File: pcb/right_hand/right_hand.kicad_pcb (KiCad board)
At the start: 2 copper layers, 160 x 110 mm, 113 parts, among them J0 UJ20-C-H-G-SMT-P16-TR, U0 SW_Push

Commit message: Fix Bluetooh Enable positioning
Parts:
- moved BLUETOOTH 0.30 mm to (190.0, 144.6)
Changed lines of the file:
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@@
 		(at 219.2375 144.6)
 		(property "Reference" "PROTOCOL"
-			(at -0.0375 -3.27 0)
+			(at -0.0375 -3.4 0)
 			(layer "F.SilkS")
 			(effects
@@
 	(footprint "snap_magic_footprints:SW_SLW-864587-2A-RA-N-D"
 		(layer "F.Cu")
-		(at 190.0375 144.3)
+		(at 190.0375 144.6)
 		(property "Reference" "BLUETOOTH"
 			(at 0.0725 -3.44 0)
@@
 	)
 	(segment
+		(start 188.0375 144.6)
+		(end 188.0375 134.6375)
+		(width 0.2)
+		(layer "F.Cu")
+		(net 80)
+	)
+	(segment
 		(start 214.4 131.2)
 		(end 217.2375 134.0375)
@@
 	)
 	(segment
-		(start 188.0375 134.6375)
-		(end 188.0375 144.3)
-		(width 0.2)
-		(layer "F.Cu")
-		(net 80)
-	)
-	(segment
 		(start 217.2375 134.0375)
 		(end 217.2375 144.6)
@@
 	)
 	(segment
-		(start 182.8 136.4)
+		(start 190.0375 144.6)
 		(end 190.0375 143.6375)
 		(width 0.2)
@@
 	)
 	(segment
-		(start 190.0375 143.6375)
-		(end 190.0375 144.3)
+		(start 182.8 136.4)
+		(end 190.0375 143.6375)
 		(width 0.2)
 		(layer "B.Cu")
@@
 			)
 		)
+	)
+	(zone
+		(net 0)
+		(net_name "")
+		(layers "F.Cu" "B.Cu")
+		(hatch edge 0.5)
+		(connect_pads
+			(clearance 0)
+		)
+		(min_thickness 0.25)
+		(filled_areas_thickness no)
+		(keepout
+			(tracks allowed)
+			(vias allowed)
+			(pads allowed)
+			(copperpour not_allowed)
+			(footprints allowed)
+		)
+		(placement
+			(enabled no)
+			(sheetname "")
+		)
+		(fill
+			(thermal_gap 0.5)
+			(thermal_bridge_width 0.5)
+		)
+		(polygon
+			(pts
+				(xy 222.4 145.4) (xy 222.4 146.8) (xy 225.2 146.8) (xy 225.2 145.4)
+			)
+		)

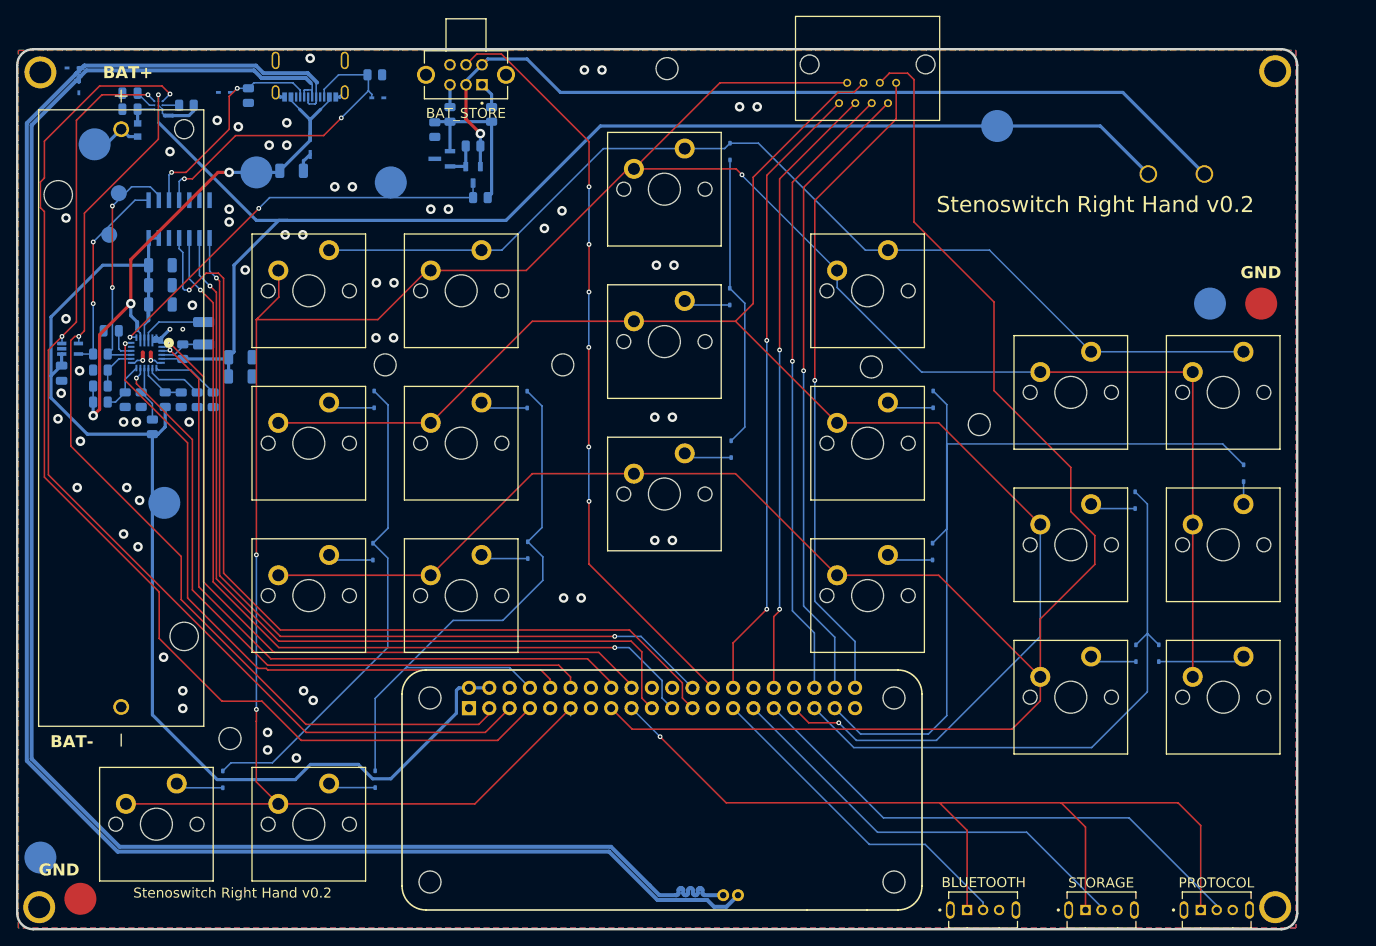
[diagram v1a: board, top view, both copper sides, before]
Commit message: Make right hand pads larger
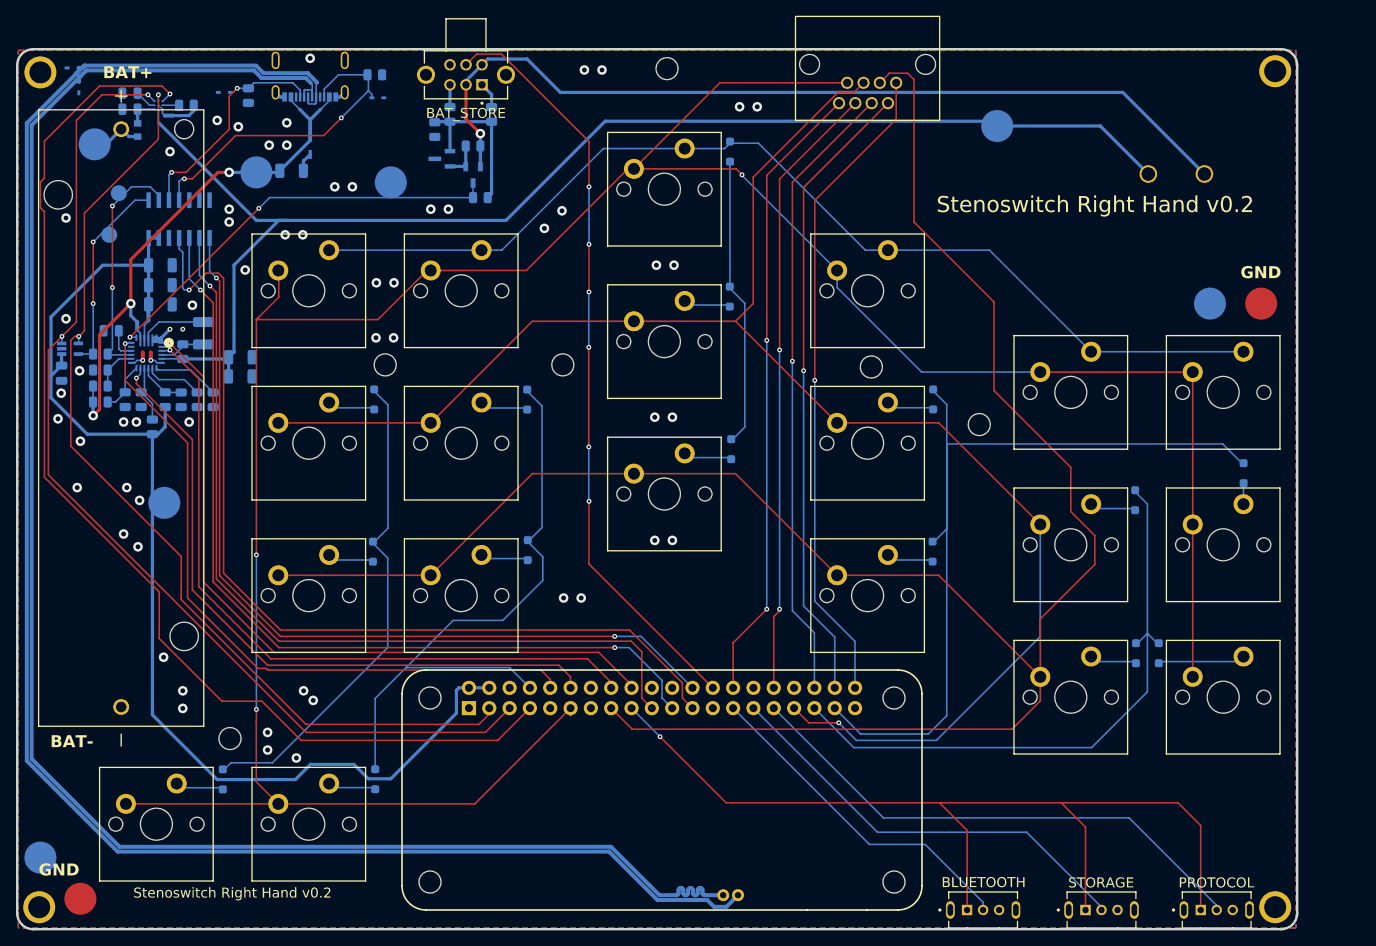
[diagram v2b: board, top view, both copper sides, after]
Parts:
- D_{AS}2, D_{AS}3, D_{B}0, D_{D}0, D_{E}0, D_{F}0, D_{G}0, D_{L}0, D_{NUM}1, D_{PR}0, D_{RR}0, D_{S}2, D_{TR}0, D_{U}0, D_{Z}0: footprint Diode_SMD:D_SOD-323 -> Diode_SMD:D_SOD-323_HandSoldering

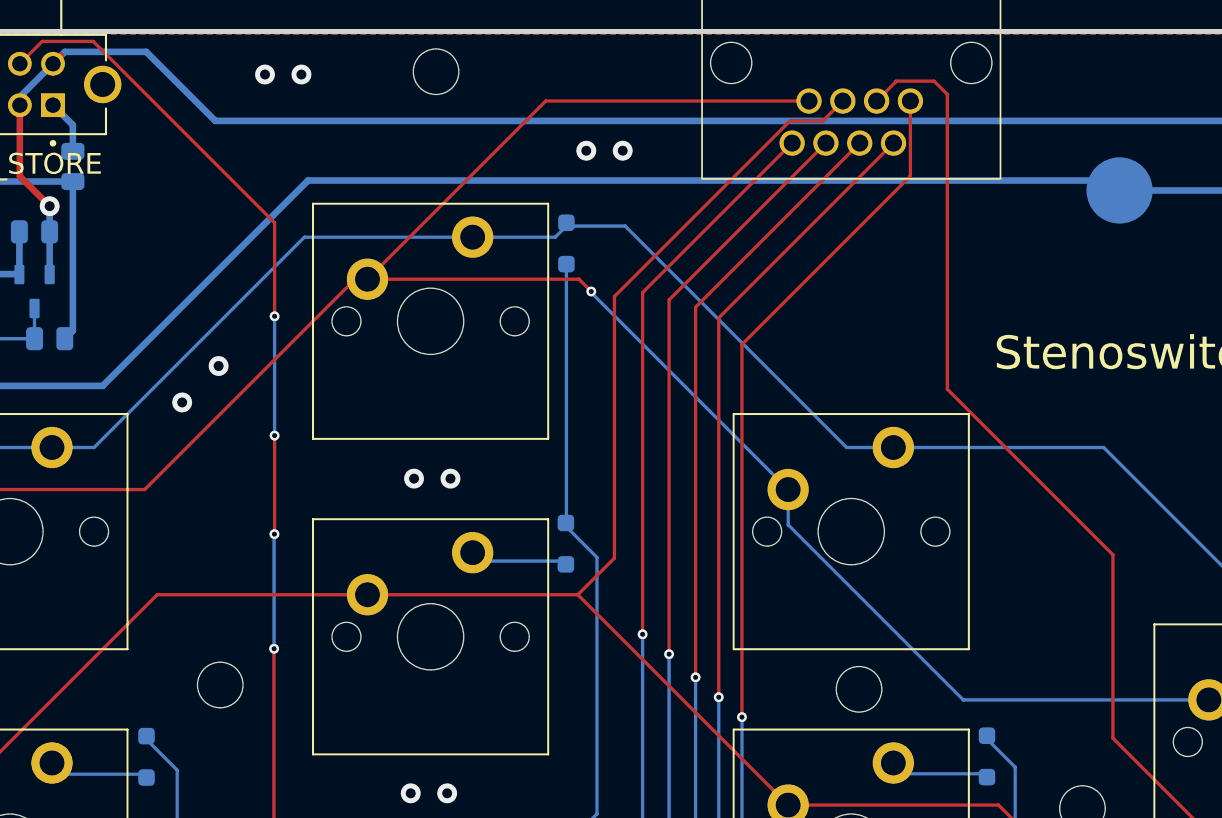
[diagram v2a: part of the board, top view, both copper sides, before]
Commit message: Right hand DRC check fixes
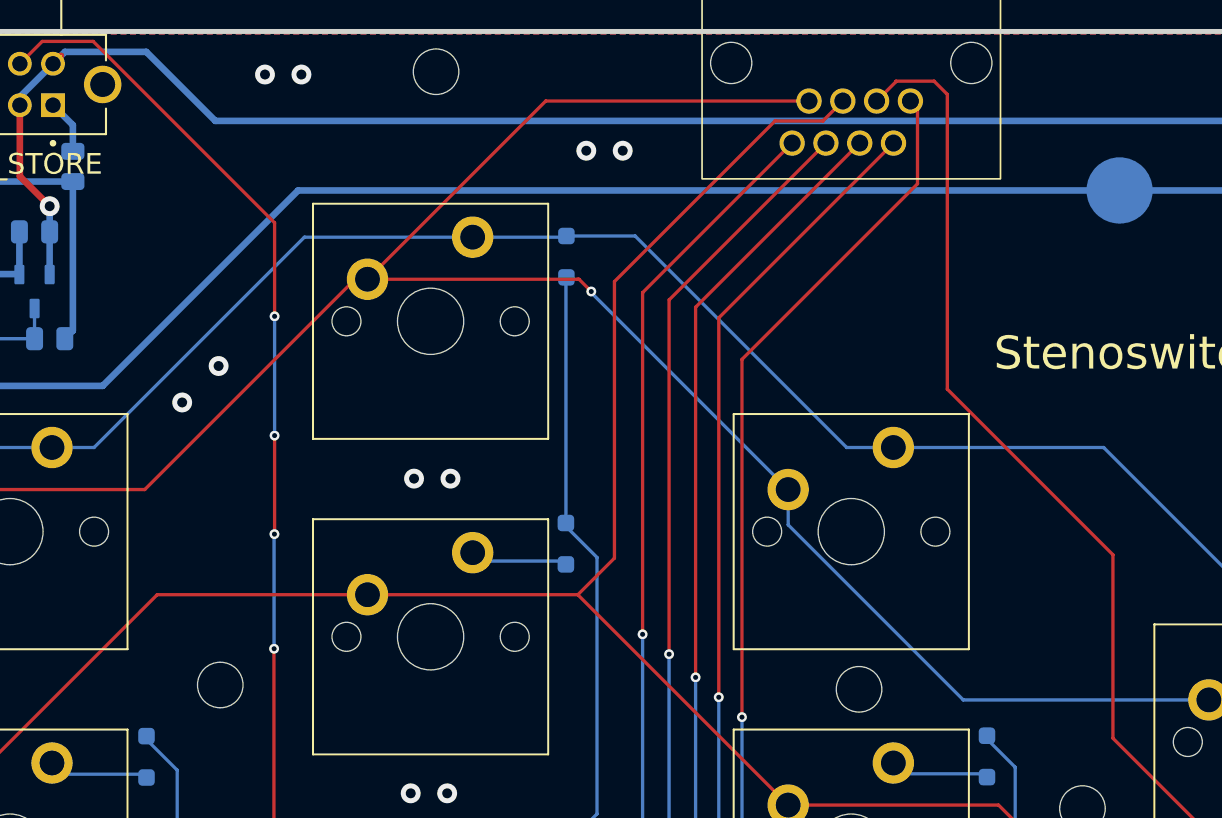
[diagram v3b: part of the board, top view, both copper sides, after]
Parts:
- moved D_{NUM}1 0.80 mm to (158.4, 50.6)
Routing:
- net /Control/Right_Columns2: track 36.6 -> 35.4 mm
- net /Rows0: track 200.8 -> 201.3 mm
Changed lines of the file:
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@@
 	(footprint "Diode_SMD:D_SOD-323_HandSoldering"
 		(layer "B.Cu")
-		(at 158.4 49.8 90)
+		(at 158.4 50.6 90)
 		(descr "SOD-323")
 		(tags "SOD-323")
@@
 	)
 	(gr_text "*"
-		(at 158.4 52.8 90)
+		(at 158.6 53.4 90)
 		(layer "B.SilkS")
 		(effects
@@
 	)
 	(segment
-		(start 173.9 42.39)
-		(end 175.09 41.2)
-		(width 0.2)
-		(layer "F.Cu")
-		(net 11)
-	)
-	(segment
-		(start 161.3 68.8)
-		(end 159.09 71.01)
+		(start 171.79 83.71)
+		(end 184.49 83.71)
 		(width 0.2)
 		(layer "F.Cu")
@@
 	)
 	(segment
-		(start 171.79 83.71)
-		(end 184.49 83.71)
+		(start 175.09 41.2)
+		(end 173.9 42.39)
 		(width 0.2)
 		(layer "F.Cu")
@@
 	)
 	(segment
-		(start 173.9 42.4)
-		(end 171.9 42.4)
+		(start 161.3 52.1)
+		(end 161.3 68.8)
 		(width 0.2)
 		(layer "F.Cu")
@@
 	(segment
 		(start 173.9 42.4)
-		(end 173.9 42.39)
+		(end 171 42.4)
 		(width 0.2)
 		(layer "F.Cu")
@@
 	)
 	(segment
-		(start 161.3 53)
-		(end 161.3 68.8)
+		(start 133.69 71.01)
+		(end 146.39 71.01)
 		(width 0.2)
 		(layer "F.Cu")
@@
 	)
 	(segment
-		(start 133.69 71.01)
-		(end 146.39 71.01)
+		(start 173.9 42.39)
+		(end 173.9 42.4)
 		(width 0.2)
 		(layer "F.Cu")
@@
 	)
 	(segment
-		(start 171.9 42.4)
-		(end 161.3 53)
+		(start 161.3 68.8)
+		(end 159.09 71.01)
 		(width 0.2)
 		(layer "F.Cu")
@@
 	)
 	(segment
+		(start 171 42.4)
+		(end 161.3 52.1)
+		(width 0.2)
+		(layer "F.Cu")
+		(net 11)
+	)
+	(segment
 		(start 175.39 41.2)
 		(end 175.1 41.2)
@@
 	)
 	(segment
-		(start 158.4 50.85)
-		(end 158.4 66.8472)
+		(start 160.2486 84.2432)
+		(end 160.2486 68.7578)
 		(width 0.2)
 		(layer "B.Cu")
@@
 	)
 	(segment
-		(start 160.2486 84.2432)
-		(end 160.2486 68.7578)
+		(start 160.2486 68.7578)
+		(end 158.369 66.8782)
 		(width 0.2)
 		(layer "B.Cu")
@@
 	)
 	(segment
-		(start 160.2486 68.7578)
-		(end 158.369 66.8782)
+		(start 158.369 66.6782)
+		(end 158.369 51.881)
 		(width 0.2)
 		(layer "B.Cu")
@@
 	)
 	(segment
-		(start 158.4 66.8472)
-		(end 158.369 66.8782)
+		(start 158.369 51.881)
+		(end 158.4 51.85)
 		(width 0.2)
 		(layer "B.Cu")
@@
 	)
 	(segment
-		(start 152.74 49.42)
-		(end 157.73 49.42)
+		(start 158.4 66.8472)
+		(end 158.369 66.8782)
 		(width 0.2)
 		(layer "B.Cu")
-		(net 34)
+		(net 33)
 	)
 	(segment
@@
 	)
 	(segment
-		(start 129.88 62.12)
-		(end 142.58 49.42)
+		(start 158.4 49.35)
+		(end 162.55 49.35)
 		(width 0.2)
 		(layer "B.Cu")
@@
 	)
 	(segment
-		(start 222.59 74.82)
-		(end 203.54 74.82)
+		(start 129.88 62.12)
+		(end 142.58 49.42)
 		(width 0.2)
 		(layer "B.Cu")
@@
 	)
 	(segment
-		(start 161.95 48.75)
-		(end 158.4 48.75)
+		(start 152.74 49.42)
+		(end 158.33 49.42)
 		(width 0.2)
 		(layer "B.Cu")
@@
 	)
 	(segment
-		(start 157.73 49.42)
-		(end 158.4 48.75)
+		(start 222.59 74.82)
+		(end 203.54 74.82)
 		(width 0.2)
 		(layer "B.Cu")
@@
 	(segment
 		(start 175.32 62.12)
-		(end 161.95 48.75)
+		(end 162.55 49.35)
 		(width 0.2)
 		(layer "B.Cu")
@@
 	)
 	(segment
+		(start 158.33 49.42)
+		(end 158.4 49.35)
+		(width 0.2)
+		(layer "B.Cu")
+		(net 34)
+	)
+	(segment
 		(start 190.84 62.12)
 		(end 203.54 74.82)
@@
 	)
 	(segment
-		(start 179.17 45.77)
-		(end 179.17 41.2)
+		(start 169 78.4)
+		(end 169 56.8)
 		(width 0.2)
 		(layer "F.Cu")
@@
 	)
 	(segment
-		(start 179.15 45.75)
-		(end 179.17 45.77)
+		(start 179.6 46.2)
+		(end 179.6 41.63)
 		(width 0.2)
 		(layer "F.Cu")
@@
 	)
 	(segment
-		(start 169 55.9)
-		(end 179.15 45.75)
+		(start 179.6 41.63)
+		(end 179.17 41.2)
 		(width 0.2)
 		(layer "F.Cu")
@@
 	)
 	(segment
-		(start 169 78.4)
-		(end 169 55.9)
+		(start 169 56.8)
+		(end 179.6 46.2)
 		(width 0.2)
 		(layer "F.Cu")
@@
 	)
 	(segment
-		(start 142.8 46)
-		(end 191.2 46)
-		(width 0.4)
-		(layer "B.Cu")
-		(net 57)
-	)
-	(segment
-		(start 130.4 58.4)
-		(end 142.8 46)
-		(width 0.4)
-		(layer "B.Cu")
-		(net 57)
-	)
-	(segment
 		(start 86.953125 46.153125)
 		(end 86.953125 44.5)
@@
 	)
 	(segment
+		(start 130.4 58.4)
+		(end 142.2 46.6)
+		(width 0.4)
+		(layer "B.Cu")
+		(net 57)
+	)
+	(segment
+		(start 142.2 46.6)
+		(end 191.8 46.6)
+		(width 0.4)
+		(layer "B.Cu")
+		(net 57)
+	)
+	(segment
+		(start 103.083436 58.4)
+		(end 130.4 58.4)
+		(width 0.4)
+		(layer "B.Cu")
+		(net 57)
+	)
+	(segment
 		(start 87 46.2)
 		(end 86.953125 46.153125)
@@
 		(width 0.4)
 		(layer "B.Cu")
-		(net 57)
-	)
-	(segment
-		(start 103.083436 58.4)
-		(end 130.4 58.4)
-		(width 0.4)
-		(layer "B.Cu")
-		(net 57)
-	)
-	(segment
-		(start 191.2 46)
-		(end 191.8 46.6)
-		(width 0.4)
-		(layer "B.Cu")
